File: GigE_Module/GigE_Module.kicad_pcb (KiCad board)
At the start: 2 copper layers, 33.5 x 25.2 mm, 5 parts, among them J1 USB_A, J2 Conn_01x10_Socket, J3 Conn_01x10_Socket, U4 ENC28J60x-SS

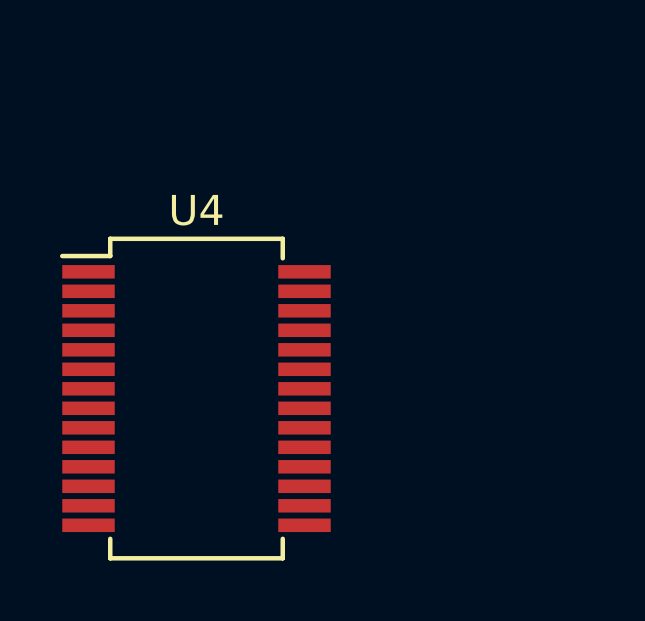
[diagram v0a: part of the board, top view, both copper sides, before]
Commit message: Adding GigE PCB design
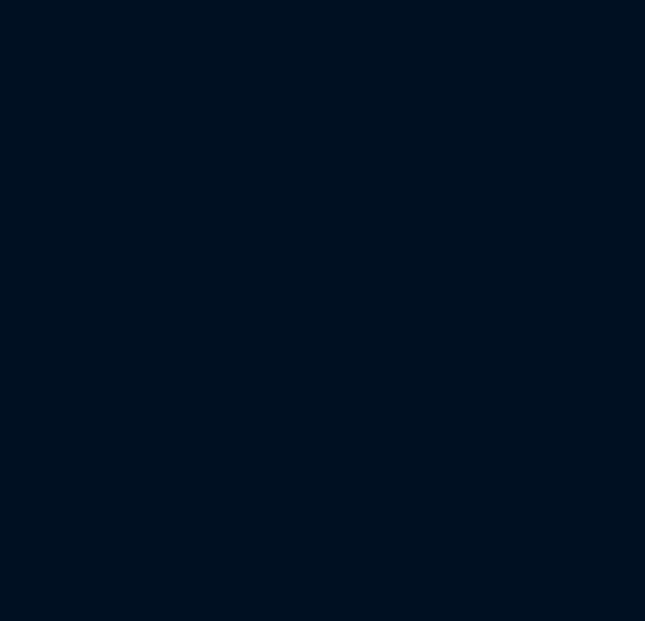
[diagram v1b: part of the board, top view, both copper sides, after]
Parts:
- removed U4: ENC28J60x-SS, Package_SO:SSOP-28_5.3x10.2mm_P0.65mm
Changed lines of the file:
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@@
   )
   (net 0 "")
-  (net 1 "unconnected-(U4-VCAP-Pad1)")
-  (net 2 "unconnected-(U4-VSS-Pad2)")
-  (net 3 "unconnected-(U4-CLKOUT-Pad3)")
-  (net 4 "unconnected-(U4-~{INT}-Pad4)")
-  (net 5 "unconnected-(U4-~{WOL}-Pad5)")
-  (net 6 "unconnected-(U4-SO-Pad6)")
-  (net 7 "unconnected-(U4-SI-Pad7)")
-  (net 8 "unconnected-(U4-SCK-Pad8)")
-  (net 9 "unconnected-(U4-~{CS}-Pad9)")
-  (net 10 "unconnected-(U4-~{RESET}-Pad10)")
-  (net 11 "unconnected-(U4-VSSRX-Pad11)")
-  (net 12 "unconnected-(U4-TPIN--Pad12)")
-  (net 13 "unconnected-(U4-TPIN+-Pad13)")
-  (net 14 "unconnected-(U4-RBIAS-Pad14)")
-  (net 15 "unconnected-(U4-VDDTX-Pad15)")
-  (net 16 "unconnected-(U4-TPOUT--Pad16)")
-  (net 17 "unconnected-(U4-TPOUT+-Pad17)")
-  (net 18 "unconnected-(U4-VSSTX-Pad18)")
-  (net 19 "unconnected-(U4-VDDRX-Pad19)")
-  (net 20 "unconnected-(U4-VDDPLL-Pad20)")
-  (net 21 "unconnected-(U4-VSSPLL-Pad21)")
-  (net 22 "unconnected-(U4-VSSOSC-Pad22)")
-  (net 23 "unconnected-(U4-OSC1-Pad23)")
-  (net 24 "unconnected-(U4-OSC2-Pad24)")
-  (net 25 "unconnected-(U4-VDDOSC-Pad25)")
-  (net 26 "unconnected-(U4-LEDB-Pad26)")
-  (net 27 "unconnected-(U4-LEDA-Pad27)")
-  (net 28 "unconnected-(U4-VDD-Pad28)")
   (footprint "Connector_PinSocket_2.00mm:PinSocket_1x10_P2.00mm_Vertical" (layer "F.Cu")
     (at 224.2412 69.1614)
@@
       (rotate (xyz 0 0 0))
     )
-  )
-  (footprint "Package_SO:SSOP-28_5.3x10.2mm_P0.65mm" (layer "F.Cu")
-    (at 136.481 99.4324)
-    (descr "28-Lead Plastic Shrink Small Outline (SS)-5.30 mm Body [SSOP] (see Microchip Packaging Specification 00000049BS.pdf)")
-    (tags "SSOP 0.65")
-    (property "Sheetfile" "GigE_Module.kicad_sch")
-    (property "Sheetname" "")
-    (property "ki_description" "ENC28J60 Single Chip Ethernet Interface, SSOP-28")
-    (property "ki_keywords" "ENC Ethernet")
-    (attr smd)
-    (fp_text reference "U4" (at 0 -6.25) (layer "F.SilkS")
-        (effects (font (size 1 1) (thickness 0.15)))
-    )
-    (fp_text value "ENC28J60x-SS" (at 0 6.25) (layer "F.Fab")
-        (effects (font (size 1 1) (thickness 0.15)))
-    )
-    (fp_text user "${REFERENCE}" (at 0 0) (layer "F.Fab")
-        (effects (font (size 0.8 0.8) (thickness 0.15)))
-    )
-    (fp_line (start -2.875 -5.325) (end -2.875 -4.75)
-      (stroke (width 0.15) (type solid)) (layer "F.SilkS"))
-    (fp_line (start -2.875 -5.325) (end 2.875 -5.325)
-      (stroke (width 0.15) (type solid)) (layer "F.SilkS"))
-    (fp_line (start -2.875 -4.75) (end -4.475 -4.75)
-      (stroke (width 0.15) (type solid)) (layer "F.SilkS"))
-    (fp_line (start -2.875 5.325) (end -2.875 4.675)
-      (stroke (width 0.15) (type solid)) (layer "F.SilkS"))
-    (fp_line (start -2.875 5.325) (end 2.875 5.325)
-      (stroke (width 0.15) (type solid)) (layer "F.SilkS"))
-    (fp_line (start 2.875 -5.325) (end 2.875 -4.675)
-      (stroke (width 0.15) (type solid)) (layer "F.SilkS"))
-    (fp_line (start 2.875 5.325) (end 2.875 4.675)
-      (stroke (width 0.15) (type solid)) (layer "F.SilkS"))
-    (fp_line (start -4.75 -5.5) (end -4.75 5.5)
-      (stroke (width 0.05) (type solid)) (layer "F.CrtYd"))
-    (fp_line (start -4.75 -5.5) (end 4.75 -5.5)
-      (stroke (width 0.05) (type solid)) (layer "F.CrtYd"))
-    (fp_line (start -4.75 5.5) (end 4.75 5.5)
-      (stroke (width 0.05) (type solid)) (layer "F.CrtYd"))
-    (fp_line (start 4.75 -5.5) (end 4.75 5.5)
-      (stroke (width 0.05) (type solid)) (layer "F.CrtYd"))
-    (fp_line (start -2.65 -4.1) (end -1.65 -5.1)
-      (stroke (width 0.15) (type solid)) (layer "F.Fab"))
-    (fp_line (start -2.65 5.1) (end -2.65 -4.1)
-      (stroke (width 0.15) (type solid)) (layer "F.Fab"))
-    (fp_line (start -1.65 -5.1) (end 2.65 -5.1)
-      (stroke (width 0.15) (type solid)) (layer "F.Fab"))
-    (fp_line (start 2.65 -5.1) (end 2.65 5.1)
-      (stroke (width 0.15) (type solid)) (layer "F.Fab"))
-    (fp_line (start 2.65 5.1) (end -2.65 5.1)
-      (stroke (width 0.15) (type solid)) (layer "F.Fab"))
-    (pad "1" smd rect (at -3.6 -4.225) (size 1.75 0.45) (layers "F.Cu" "F.Paste" "F.Mask")
-      (net 1 "unconnected-(U4-VCAP-Pad1)") (pinfunction "VCAP") (pintype "input"))
-    (pad "2" smd rect (at -3.6 -3.575) (size 1.75 0.45) (layers "F.Cu" "F.Paste" "F.Mask")
-      (net 2 "unconnected-(U4-VSS-Pad2)") (pinfunction "VSS") (pintype "power_in"))
-    (pad "3" smd rect (at -3.6 -2.925) (size 1.75 0.45) (layers "F.Cu" "F.Paste" "F.Mask")
-      (net 3 "unconnected-(U4-CLKOUT-Pad3)") (pinfunction "CLKOUT") (pintype "output"))
-    (pad "4" smd rect (at -3.6 -2.275) (size 1.75 0.45) (layers "F.Cu" "F.Paste" "F.Mask")
-      (net 4 "unconnected-(U4-~{INT}-Pad4)") (pinfunction "~{INT}") (pintype "output"))
-    (pad "5" smd rect (at -3.6 -1.625) (size 1.75 0.45) (layers "F.Cu" "F.Paste" "F.Mask")
-      (net 5 "unconnected-(U4-~{WOL}-Pad5)") (pinfunction "~{WOL}") (pintype "output"))
-    (pad "6" smd rect (at -3.6 -0.975) (size 1.75 0.45) (layers "F.Cu" "F.Paste" "F.Mask")
-      (net 6 "unconnected-(U4-SO-Pad6)") (pinfunction "SO") (pintype "output"))
-    (pad "7" smd rect (at -3.6 -0.325) (size 1.75 0.45) (layers "F.Cu" "F.Paste" "F.Mask")
-      (net 7 "unconnected-(U4-SI-Pad7)") (pinfunction "SI") (pintype "input"))
-    (pad "8" smd rect (at -3.6 0.325) (size 1.75 0.45) (layers "F.Cu" "F.Paste" "F.Mask")
-      (net 8 "unconnected-(U4-SCK-Pad8)") (pinfunction "SCK") (pintype "input"))
-    (pad "9" smd rect (at -3.6 0.975) (size 1.75 0.45) (layers "F.Cu" "F.Paste" "F.Mask")
-      (net 9 "unconnected-(U4-~{CS}-Pad9)") (pinfunction "~{CS}") (pintype "input"))
-    (pad "10" smd rect (at -3.6 1.625) (size 1.75 0.45) (layers "F.Cu" "F.Paste" "F.Mask")
-      (net 10 "unconnected-(U4-~{RESET}-Pad10)") (pinfunction "~{RESET}") (pintype "input"))
-    (pad "11" smd rect (at -3.6 2.275) (size 1.75 0.45) (layers "F.Cu" "F.Paste" "F.Mask")
-      (net 11 "unconnected-(U4-VSSRX-Pad11)") (pinfunction "VSSRX") (pintype "power_in"))
-    (pad "12" smd rect (at -3.6 2.925) (size 1.75 0.45) (layers "F.Cu" "F.Paste" "F.Mask")
-      (net 12 "unconnected-(U4-TPIN--Pad12)") (pinfunction "TPIN-") (pintype "input"))
-    (pad "13" smd rect (at -3.6 3.575) (size 1.75 0.45) (layers "F.Cu" "F.Paste" "F.Mask")
-      (net 13 "unconnected-(U4-TPIN+-Pad13)") (pinfunction "TPIN+") (pintype "input"))
-    (pad "14" smd rect (at -3.6 4.225) (size 1.75 0.45) (layers "F.Cu" "F.Paste" "F.Mask")
-      (net 14 "unconnected-(U4-RBIAS-Pad14)") (pinfunction "RBIAS") (pintype "input"))
-    (pad "15" smd rect (at 3.6 4.225) (size 1.75 0.45) (layers "F.Cu" "F.Paste" "F.Mask")
-      (net 15 "unconnected-(U4-VDDTX-Pad15)") (pinfunction "VDDTX") (pintype "power_in"))
-    (pad "16" smd rect (at 3.6 3.575) (size 1.75 0.45) (layers "F.Cu" "F.Paste" "F.Mask")
-      (net 16 "unconnected-(U4-TPOUT--Pad16)") (pinfunction "TPOUT-") (pintype "output"))
-    (pad "17" smd rect (at 3.6 2.925) (size 1.75 0.45) (layers "F.Cu" "F.Paste" "F.Mask")
-      (net 17 "unconnected-(U4-TPOUT+-Pad17)") (pinfunction "TPOUT+") (pintype "output"))
-    (pad "18" smd rect (at 3.6 2.275) (size 1.75 0.45) (layers "F.Cu" "F.Paste" "F.Mask")
-      (net 18 "unconnected-(U4-VSSTX-Pad18)") (pinfunction "VSSTX") (pintype "power_in"))
-    (pad "19" smd rect (at 3.6 1.625) (size 1.75 0.45) (layers "F.Cu" "F.Paste" "F.Mask")
-      (net 19 "unconnected-(U4-VDDRX-Pad19)") (pinfunction "VDDRX") (pintype "power_in"))
-    (pad "20" smd rect (at 3.6 0.975) (size 1.75 0.45) (layers "F.Cu" "F.Paste" "F.Mask")
-      (net 20 "unconnected-(U4-VDDPLL-Pad20)") (pinfunction "VDDPLL") (pintype "power_in"))
-    (pad "21" smd rect (at 3.6 0.325) (size 1.75 0.45) (layers "F.Cu" "F.Paste" "F.Mask")
-      (net 21 "unconnected-(U4-VSSPLL-Pad21)") (pinfunction "VSSPLL") (pintype "power_in"))
-    (pad "22" smd rect (at 3.6 -0.325) (size 1.75 0.45) (layers "F.Cu" "F.Paste" "F.Mask")
-      (net 22 "unconnected-(U4-VSSOSC-Pad22)") (pinfunction "VSSOSC") (pintype "power_in"))
-    (pad "23" smd rect (at 3.6 -0.975) (size 1.75 0.45) (layers "F.Cu" "F.Paste" "F.Mask")
-      (net 23 "unconnected-(U4-OSC1-Pad23)") (pinfunction "OSC1") (pintype "input"))
-    (pad "24" smd rect (at 3.6 -1.625) (size 1.75 0.45) (layers "F.Cu" "F.Paste" "F.Mask")
-      (net 24 "unconnected-(U4-OSC2-Pad24)") (pinfunction "OSC2") (pintype "input"))
-    (pad "25" smd rect (at 3.6 -2.275) (size 1.75 0.45) (layers "F.Cu" "F.Paste" "F.Mask")
-      (net 25 "unconnected-(U4-VDDOSC-Pad25)") (pinfunction "VDDOSC") (pintype "power_in"))
-    (pad "26" smd rect (at 3.6 -2.925) (size 1.75 0.45) (layers "F.Cu" "F.Paste" "F.Mask")
-      (net 26 "unconnected-(U4-LEDB-Pad26)") (pinfunction "LEDB") (pintype "output"))
-    (pad "27" smd rect (at 3.6 -3.575) (size 1.75 0.45) (layers "F.Cu" "F.Paste" "F.Mask")
-      (net 27 "unconnected-(U4-LEDA-Pad27)") (pinfunction "LEDA") (pintype "output"))
-    (pad "28" smd rect (at 3.6 -4.225) (size 1.75 0.45) (layers "F.Cu" "F.Paste" "F.Mask")
-      (net 28 "unconnected-(U4-VDD-Pad28)") (pinfunction "VDD") (pintype "power_in"))
-    (model "${KICAD6_3DMODEL_DIR}/Package_SO.3dshapes/SSOP-28_5.3x10.2mm_P0.65mm.wrl"
-      (offset (xyz 0 0 0))
-      (scale (xyz 1 1 1))
-      (rotate (xyz 0 0 0))
-    )

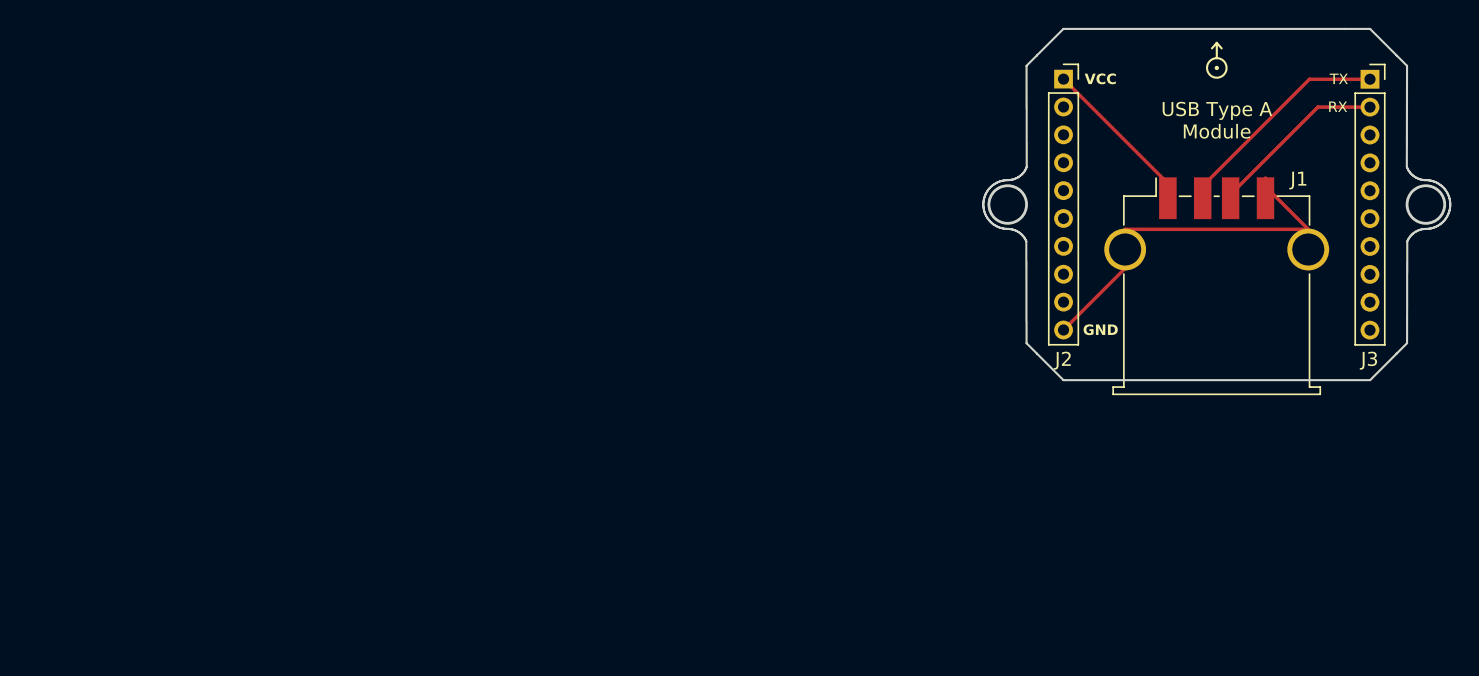
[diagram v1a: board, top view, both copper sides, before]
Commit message: Adding first version of GigE PCB design
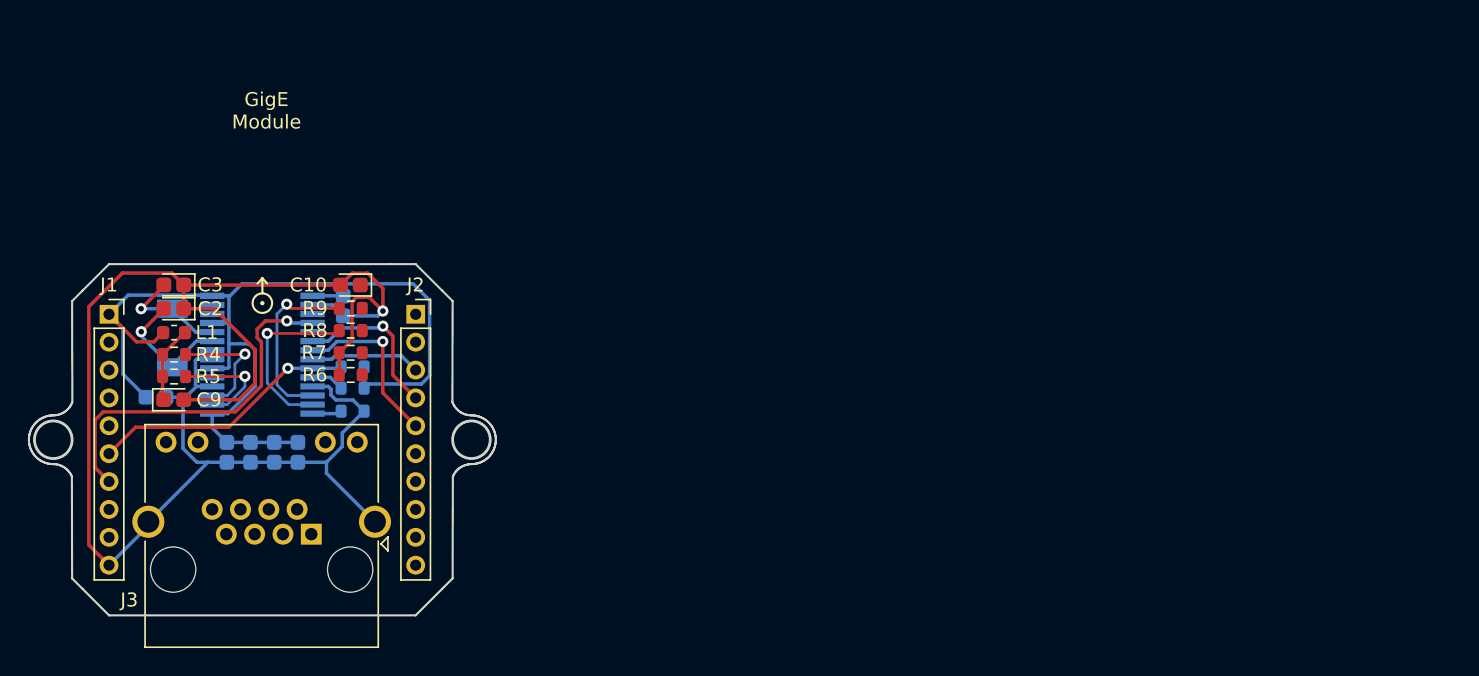
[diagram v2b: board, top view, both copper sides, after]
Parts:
- added C1: 10uF, Capacitor_Tantalum_SMD:CP_EIA-1608-08_AVX-J, B.Cu at (150.6, 85.4)
- added C10: 10nF, Capacitor_Tantalum_SMD:CP_EIA-1608-08_AVX-J, F.Cu at (151.1, 83.9)
- added C2: 18pF, Capacitor_Tantalum_SMD:CP_EIA-1608-08_AVX-J, F.Cu at (138.4, 85.6)
- added C3: 18pF, Capacitor_Tantalum_SMD:CP_EIA-1608-08_AVX-J, F.Cu at (138.4, 83.9)
- added C4: 100nF, Capacitor_Tantalum_SMD:CP_EIA-1608-08_AVX-J, B.Cu at (137.1, 92.0)
- added C5: 100nF, Capacitor_Tantalum_SMD:CP_EIA-1608-08_AVX-J, B.Cu at (142.2, 95.9)
- added C6: 100nF, Capacitor_Tantalum_SMD:CP_EIA-1608-08_AVX-J, B.Cu at (143.9, 95.9)
- added C7: 100nF, Capacitor_Tantalum_SMD:CP_EIA-1608-08_AVX-J, B.Cu at (145.6, 95.9)
- added C8: 100nF, Capacitor_Tantalum_SMD:CP_EIA-1608-08_AVX-J, B.Cu at (147.3, 95.9)
- added C9: 0.01u, Capacitor_Tantalum_SMD:CP_EIA-1608-08_AVX-J, F.Cu at (138.4, 92.2)
- added L1: 10uH, Inductor_SMD:L_0603_1608Metric, F.Cu at (138.4, 87.3)
- added R1: 100k, Resistor_SMD:R_0603_1608Metric, B.Cu at (151.2, 89.8)
- added R2: 10k, Resistor_SMD:R_0603_1608Metric, B.Cu at (151.2, 91.3)
- added R3: 2k, Resistor_SMD:R_0603_1608Metric, B.Cu at (151.2, 93.0)
- added R4: 49.9, Resistor_SMD:R_0603_1608Metric, F.Cu at (138.4, 88.9)
- added R5: 49.9, Resistor_SMD:R_0603_1608Metric, F.Cu at (138.4, 90.5)
- added R6: 180, Resistor_SMD:R_0603_1608Metric, F.Cu at (151.1, 90.4)
- added R7: 180, Resistor_SMD:R_0603_1608Metric, F.Cu at (151.1, 88.8)
- added R8: 49.9, Resistor_SMD:R_0603_1608Metric, F.Cu at (151.1, 87.2)
- added R9: 49.9, Resistor_SMD:R_0603_1608Metric, F.Cu at (151.1, 85.6)
- added U4: ENC28J60x-SS, Package_SO:SSOP-28_5.3x10.2mm_P0.65mm, B.Cu at (144.8, 88.9)
- added Y1: 25MHz, Crystal:Crystal_SMD_MicroCrystal_CC4V-T1A-2Pin_5.0x1.9mm, B.Cu at (138.3, 87.7)
- J1: value USB_A -> Conn_01x10_Socket; footprint Connector_USB:USB_A_TE_292303-7_Horizontal -> Connector_PinSocket_2.00mm:PinSocket_1x10_P2.00mm_Vertical
- J3: value Conn_01x10_Socket -> RJ45_Amphenol_RJMG1BD3B8K1ANR; footprint Connector_PinSocket_2.00mm:PinSocket_1x10_P2.00mm_Vertical -> Connector_RJ:RJ45_Amphenol_RJHSE538X
- moved J3 82.7 mm to (148.3, 101.8), turned to 180 degrees
- moved J1 79.5 mm to (133.8, 86.0)
- moved EXP_ORIENTATION 70.5 mm to (144.8, 85.2)
- moved J2 49.4 mm to (155.8, 86.0)
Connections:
- J1 pad 1: (no net) -> /VCC
- J1 pad 2: (no net) -> unconnected-(J1-Pin_2-Pad2)
- J1 pad 3: (no net) -> unconnected-(J1-Pin_3-Pad3)
- J1 pad 4: (no net) -> unconnected-(J1-Pin_4-Pad4)
- J1 pad 5: (no net) -> unconnected-(J1-Pin_5-Pad5)
- J2 pad 1: (no net) -> unconnected-(J2-Pin_1-Pad1)
- J2 pad 10: (no net) -> unconnected-(J2-Pin_10-Pad10)
- J2 pad 2: (no net) -> unconnected-(J2-Pin_2-Pad2)
- J2 pad 3: (no net) -> /SCK
- J2 pad 4: (no net) -> /MISO
- J2 pad 5: (no net) -> /MOSI
- J2 pad 6: (no net) -> unconnected-(J2-Pin_6-Pad6)
- J2 pad 7: (no net) -> unconnected-(J2-Pin_7-Pad7)
- J2 pad 8: (no net) -> unconnected-(J2-Pin_8-Pad8)
- J2 pad 9: (no net) -> unconnected-(J2-Pin_9-Pad9)
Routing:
- net /GND: track 0.00 -> 121.8 mm, vias 0 -> 1
- net /VCC: track 0.00 -> 73.2 mm
- net (no net): track 68.8 -> 0.00 mm
- net /INT: track 0.00 -> 26.2 mm, vias 0 -> 1
- net /CS: track 0.00 -> 19.2 mm, vias 0 -> 1
- net /TPIN-: track 0.00 -> 13.1 mm, vias 0 -> 1
- net /TPIN+: track 0.00 -> 12.7 mm, vias 0 -> 1
- net /MOSI: track 0.00 -> 12.3 mm, vias 0 -> 1
- net /MISO: track 0.00 -> 11.6 mm, vias 0 -> 1
- net Net-(U4-OSC1): track 0.00 -> 9.51 mm, vias 0 -> 1
- net /TPOUT+: track 0.00 -> 8.85 mm, vias 0 -> 1
- net Net-(U4-OSC2): track 0.00 -> 8.18 mm, vias 0 -> 1
- net /SCK: track 0.00 -> 7.93 mm
- net /TPOUT-: track 0.00 -> 7.89 mm, vias 0 -> 1
- net Net-(J3-TCT): track 0.00 -> 5.55 mm
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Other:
- outline, holes or cut-outs redrawn
- board text added: "GigE Module"
- board text removed: "GND"
- board text removed: "RX"
- board text removed: "TX"
- board text removed: "USB Type A Module"
- board text removed: "VCC"

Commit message: Finishing GigE PCB design
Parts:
- removed EXP_ORIENTATION: VAL**, bitcraze:EXP_ORIENTATION
- C2, C3, C9, L1, R4, R5: moved to B.Cu
- J3: value RJ45_Amphenol_RJMG1BD3B8K1ANR -> RJ45_LED
- moved R5 15.2 mm to (151.2, 98.7)
- moved R4 15.2 mm to (151.2, 97.0)
- moved L1 11.3 mm to (138.3, 98.7)
- moved C5 8.64 mm to (141.9, 104.6)
- moved C8 8.64 mm to (147.6, 104.6)
- moved C6 8.63 mm to (143.8, 104.6)
- moved C7 8.63 mm to (145.7, 104.6)
- moved C10 4.98 mm to (151.1, 88.9), turned to 0 degrees
- moved R9 4.98 mm to (151.1, 90.6)
- moved R8 4.97 mm to (151.1, 92.2), turned to 0 degrees
- moved C9 4.87 mm to (138.3, 97.0), turned to 180 degrees
- moved C2 4.46 mm to (136.1, 89.4), turned to -90 degrees
- moved R7 3.46 mm to (151.1, 85.3), turned to 0 degrees
- moved R6 3.45 mm to (151.1, 86.9), turned to 0 degrees
- moved C3 3.29 mm to (136.1, 86.2), turned to 90 degrees
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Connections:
- C9 pad 1: Net-(J3-TCT) -> Net-(C9-Pad1)
- J3 pad 1: (no net) -> /TPOUT+
- J3 pad 10: (no net) -> /LEDB
- J3 pad 11: (no net) -> Net-(J3-Pad11)
- J3 pad 12: (no net) -> /LEDA
- J3 pad 2: (no net) -> /TPOUT-
- J3 pad 3: (no net) -> /TPIN+
- J3 pad 4: (no net) -> Net-(C9-Pad1)
- J3 pad 5: (no net) -> unconnected-(J3-Pad5)
- J3 pad 6: (no net) -> /TPIN-
- J3 pad 7: (no net) -> unconnected-(J3-Pad7)
- J3 pad 8: (no net) -> unconnected-(J3-Pad8)
- J3 pad 9: (no net) -> Net-(J3-Pad9)
- J3 pad SH: /GND -> (no net)
- L1 pad 2: Net-(J3-TCT) -> Net-(C9-Pad1)
- R4 pad 1: Net-(J3-TCT) -> Net-(C9-Pad1)
- R5 pad 2: Net-(J3-TCT) -> Net-(C9-Pad1)
- R6 pad 1: Net-(J3-PadL1) -> Net-(J3-Pad11)
- R7 pad 1: Net-(J3-PadL3) -> Net-(J3-Pad9)
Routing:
- net /LEDB: track 0.00 -> 28.5 mm, vias 0 -> 1
- net /VCC: track 73.2 -> 98.2 mm, vias 0 -> 2
- net /GND: track 121.8 -> 100.4 mm, vias 1 -> 7
- net /LEDA: track 0.00 -> 19.5 mm, vias 0 -> 2
- net Net-(C9-Pad1): track 0.00 -> 15.8 mm
- net Net-(J3-Pad9): track 0.00 -> 13.8 mm
- net Net-(J3-Pad11): track 0.00 -> 13.8 mm
- net /MISO: track 11.6 -> 24.7 mm, vias 1 -> 0
- net /TPOUT+: track 8.85 -> 21.6 mm
- net /TPIN+: track 12.7 -> 24.0 mm
- net /TPOUT-: track 7.89 -> 16.0 mm
- net Net-(J3-TCT): track 5.55 -> 0.00 mm
- net Net-(C10-Pad1): track 0.00 -> 4.61 mm
- net /CS: track 19.2 -> 23.7 mm
- net /INT: track 26.2 -> 22.1 mm
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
